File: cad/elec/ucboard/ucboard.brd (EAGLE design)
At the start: 34 x 14 mm, 14 parts

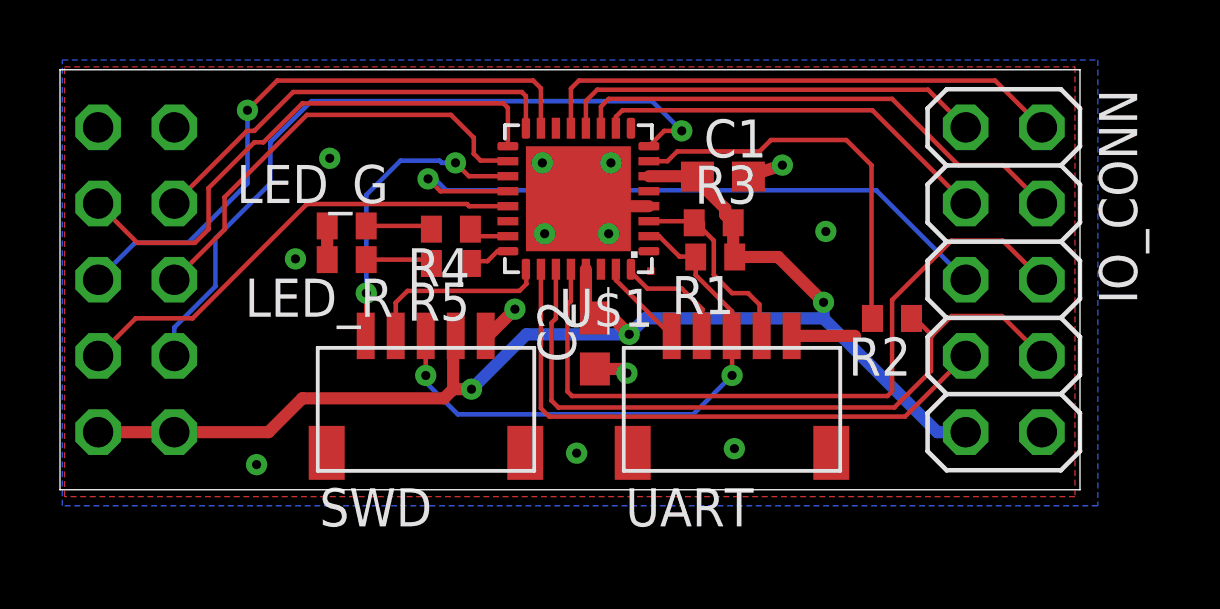
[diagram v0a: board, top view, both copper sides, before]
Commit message: added two solder bridges to be attach ether the 8 pin transceiver or the 10 pin transceiver (they are almost pin compatible) and exchanged the connectors for dummy 0.05 inch holes. A debug/flash utility can be built more easily
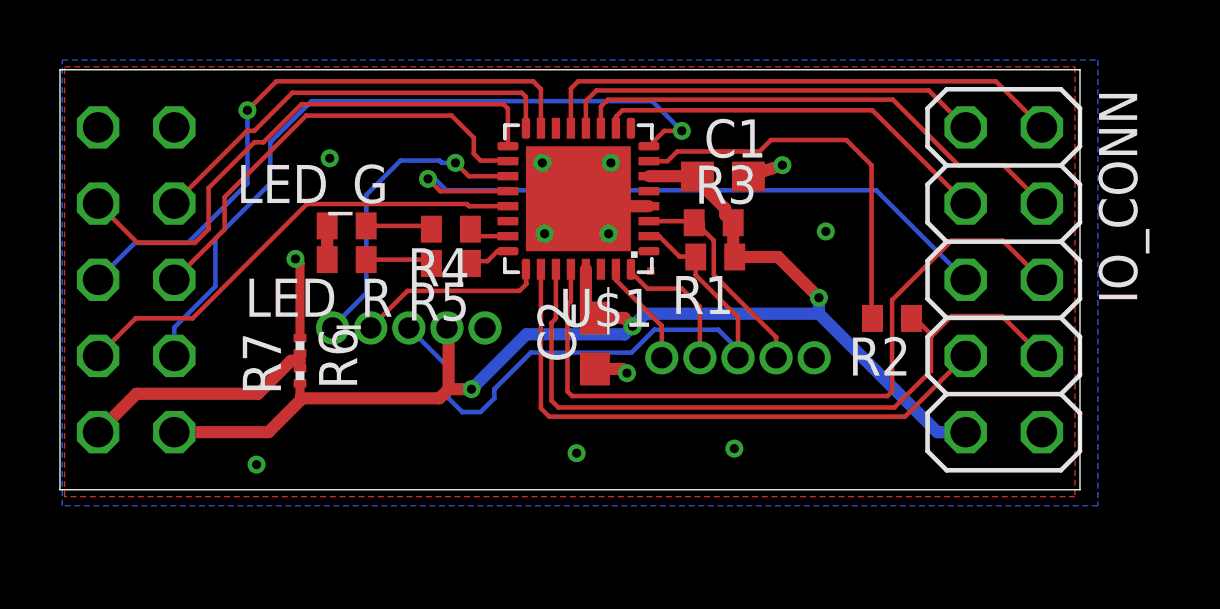
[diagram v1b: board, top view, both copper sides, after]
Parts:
- removed SWD: 5PIN, te_1mm_connector:5PIN
- added DBG: (no value), viskos:05HEADER
- added R6, R7: 0R/NA, rcl:R0201
- UART: value 5PIN -> (none); device te_1mm_connector:5PIN -> viskos:05HEADER
- moved UART 0.73 mm to (22.6, 4.40)
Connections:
- new net N$4: R6.2, R7.2, RF_CONN.1
- net +3V3: now also DBG.P$4, R7.1; no longer RF_CONN.1, SWD.P$4
- net GND: now also DBG.P$5, R6.1; no longer SWD.P$5
- net RESET: now also DBG.P$3; no longer SWD.P$3
- net SWCLK: now also DBG.P$1; no longer SWD.P$1
- net SWDIO: now also DBG.P$2; no longer SWD.P$2
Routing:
- net N$4: track 0.00 -> 8.21 mm
- net +3V3: track 45.9 -> 44.1 mm
- net RESET: track 19.0 -> 20.4 mm, vias 2 -> 0
- net GND: track 11.1 -> 10.4 mm, vias 13 -> 12
- net TXD: track 3.89 -> 4.57 mm
- net ISP_ENABLE: track 6.71 -> 7.33 mm
- net RXD: track 2.99 -> 3.58 mm
- net SWCLK: track 10.1 -> 10.3 mm, vias 2 -> 1

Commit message: added new battery powered board and changed lots of other stuff
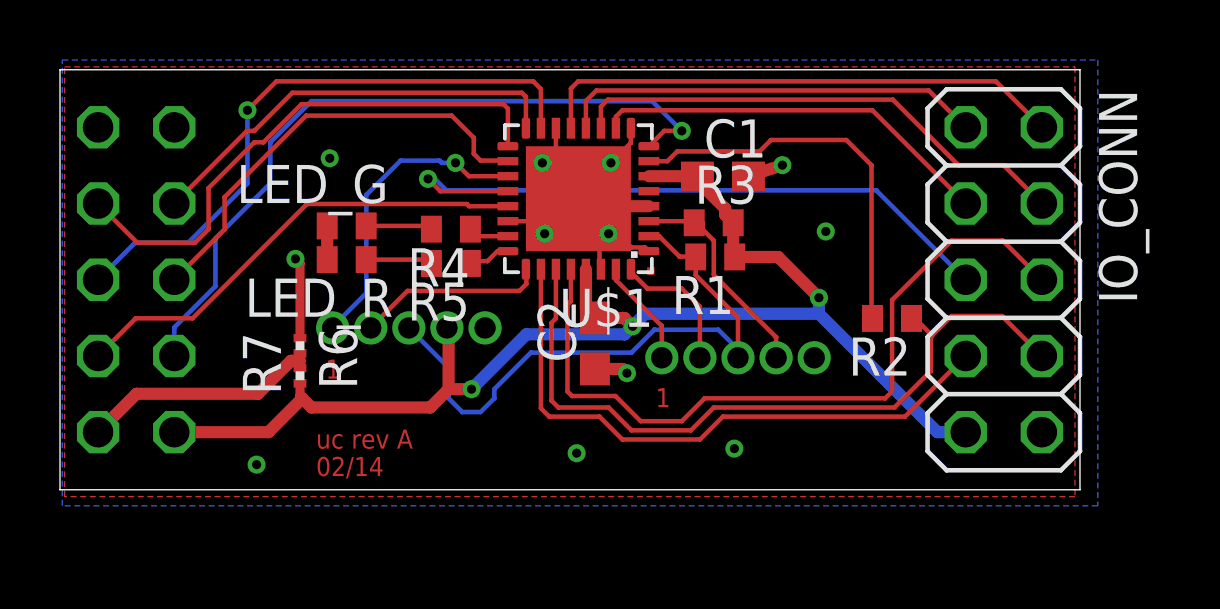
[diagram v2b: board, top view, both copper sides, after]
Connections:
- net GND: now also U$1.1, U$1.14, U$1.22, U$1.30, U$1.9
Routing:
- net GND: track 10.4 -> 17.4 mm
- net IO_5: track 24.5 -> 25.2 mm
- net IO_ID: track 24.3 -> 24.9 mm
- net IO_6: track 19.7 -> 20.4 mm
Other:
- board text added: "02/14"
- board text added: "1"
- board text added: "FEMALE BOTTOM"
- board text added: "MALE TOP"
- board text added: "uc rev A"
